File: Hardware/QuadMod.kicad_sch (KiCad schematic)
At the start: 30 parts, among them J6 SWD_Header, U1 STM32H563VIT, U2 AK4619VN, Y1 8MHz 20pF

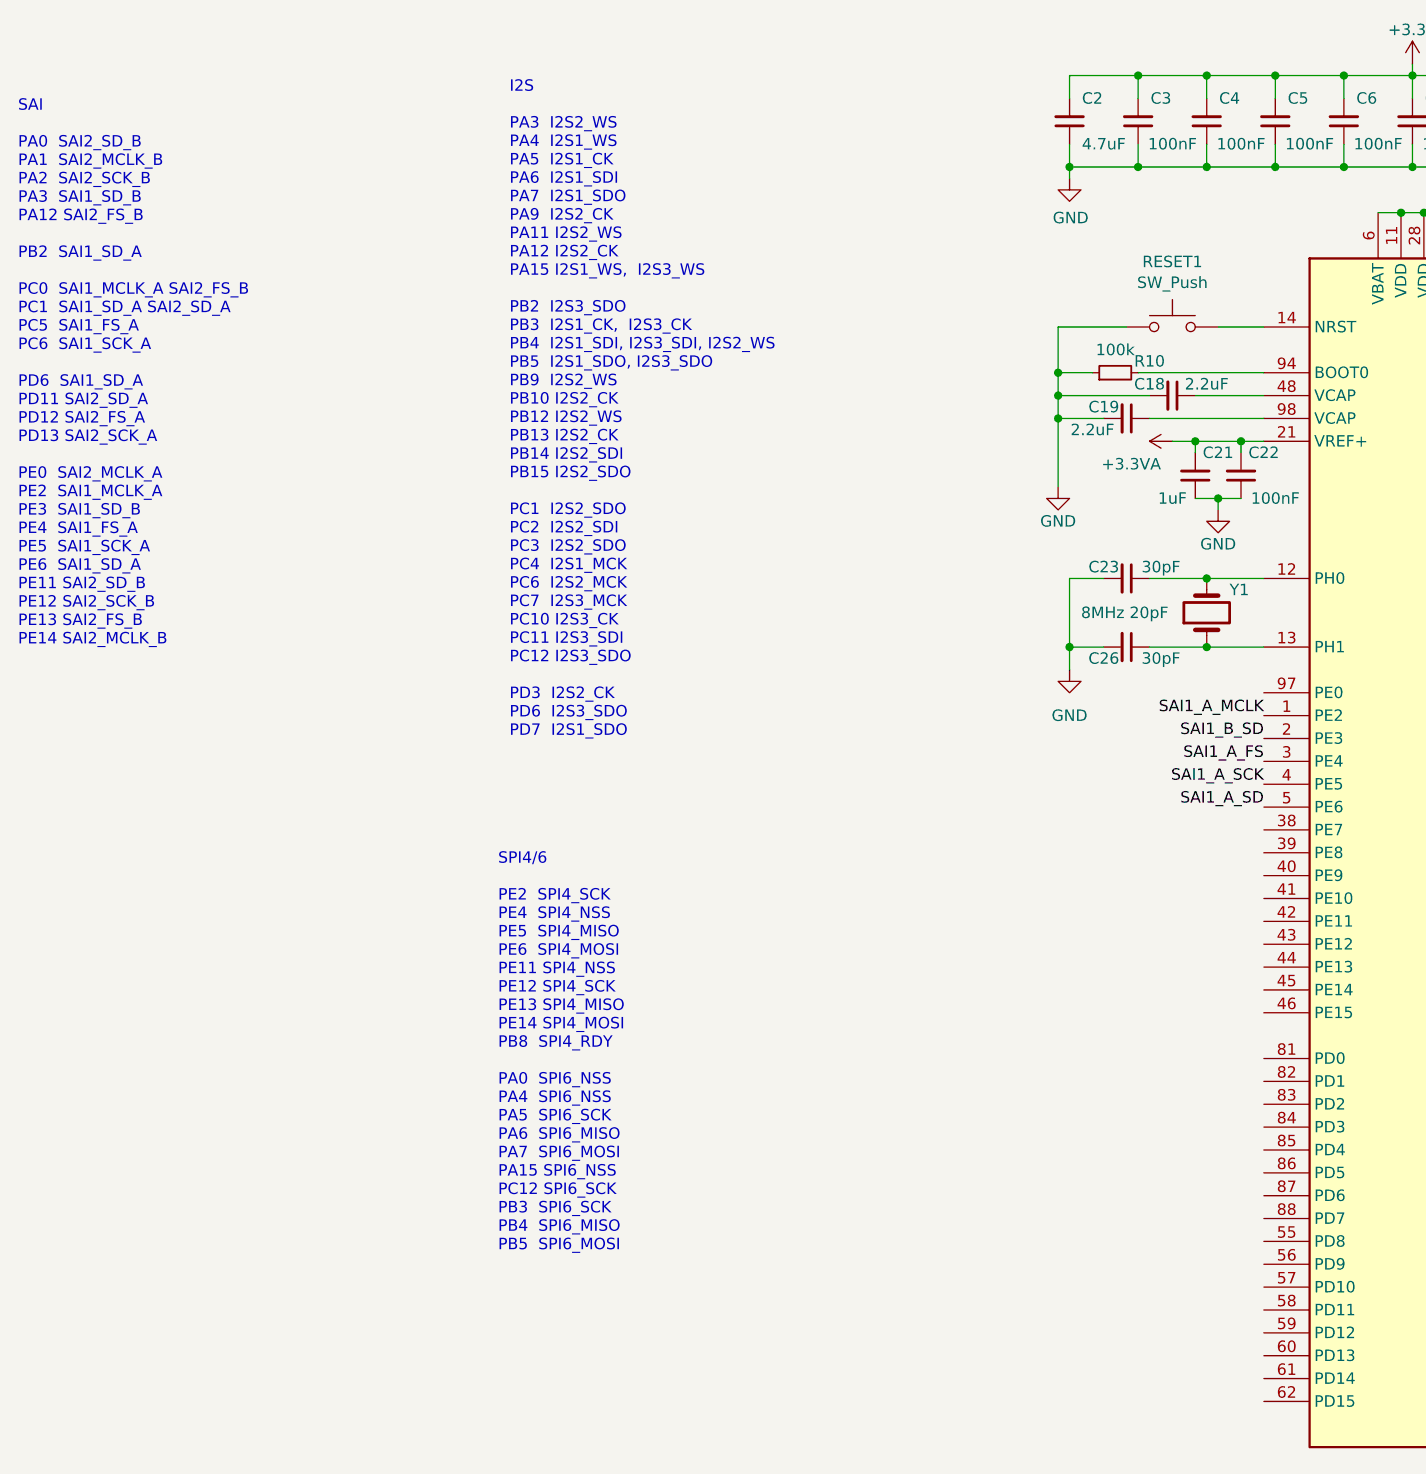
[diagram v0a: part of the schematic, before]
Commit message: Started configuring SAI2
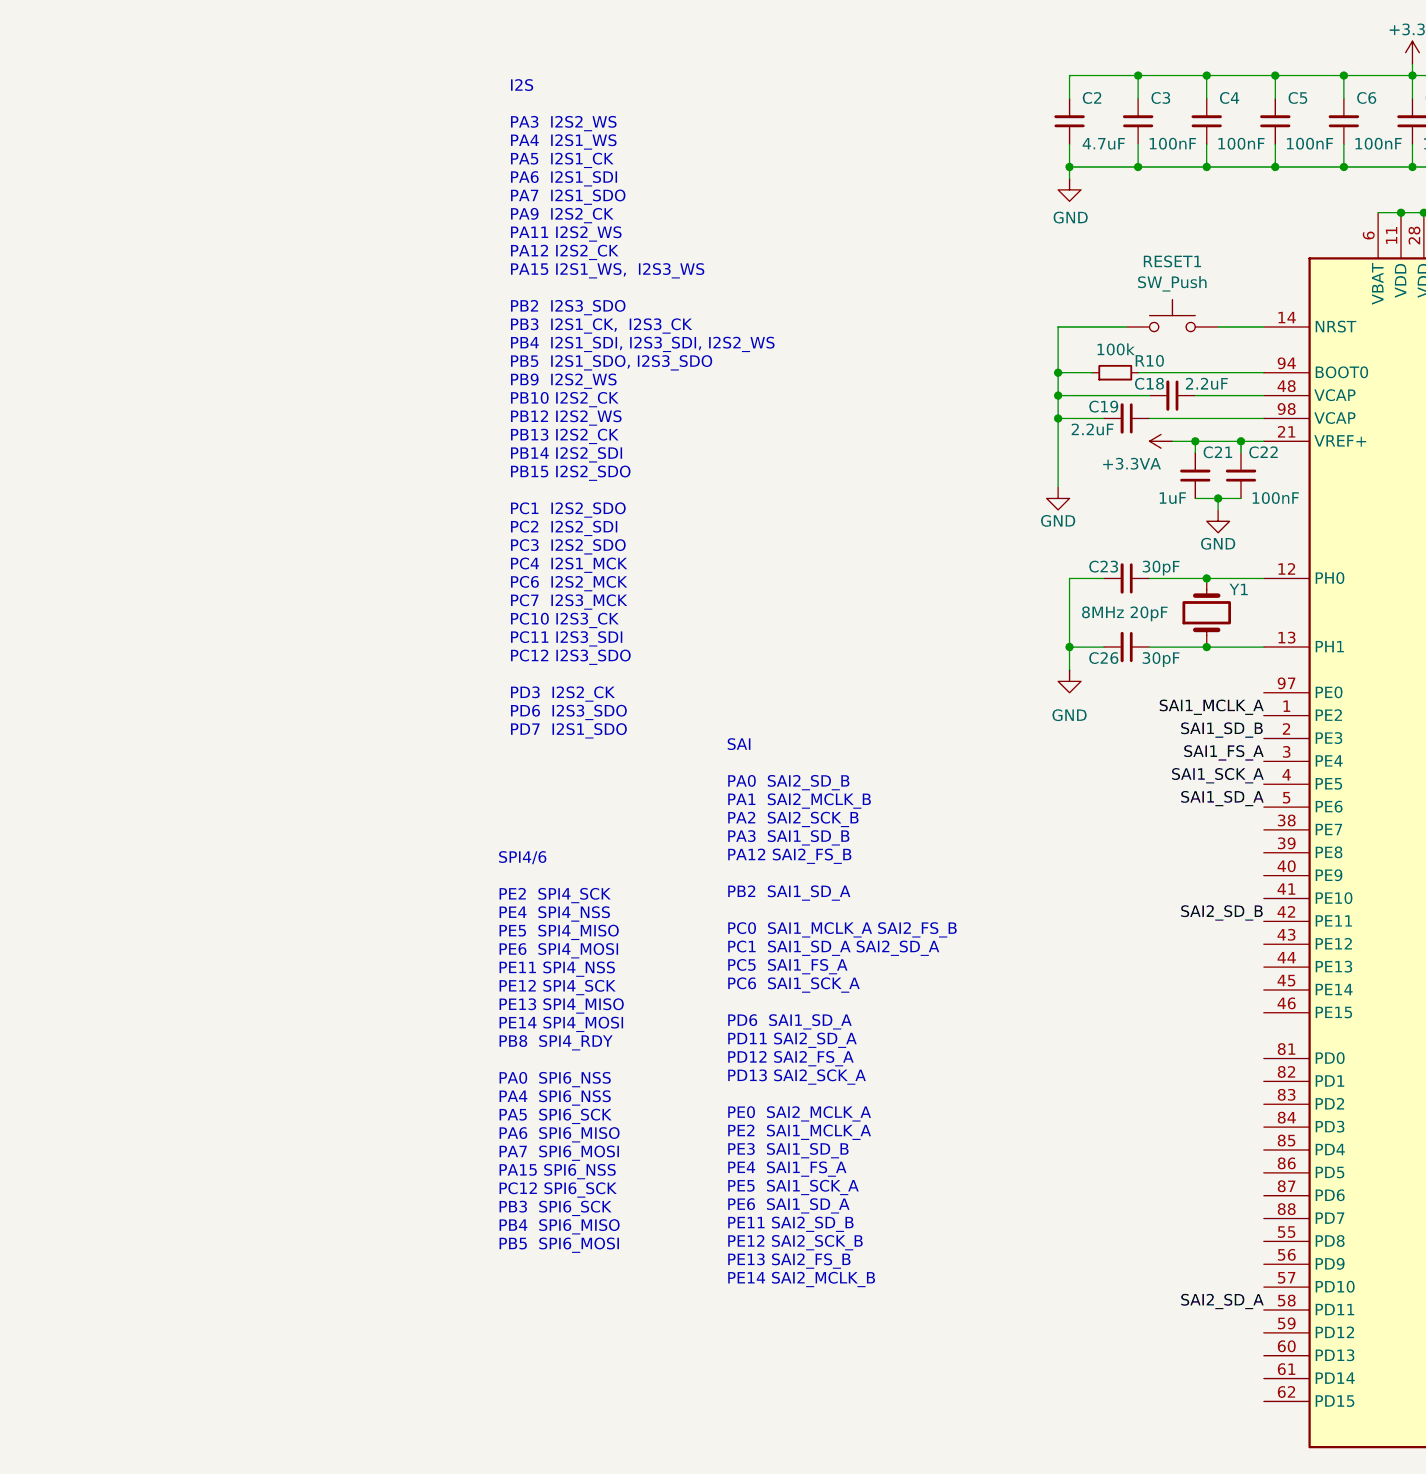
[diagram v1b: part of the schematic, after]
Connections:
- net SAI2_SD_B: now reaches U1.42 (PE11)
- net SAI2_SD_A: now reaches U1.58 (PD11)
- net SAI1_A_FS renamed SAI1_FS_A
- net SAI1_A_MCLK renamed SAI1_MCLK_A
- net SAI1_A_SCK renamed SAI1_SCK_A
- net SAI1_A_SD renamed SAI1_SD_A
- net SAI1_B_SD renamed SAI1_SD_B

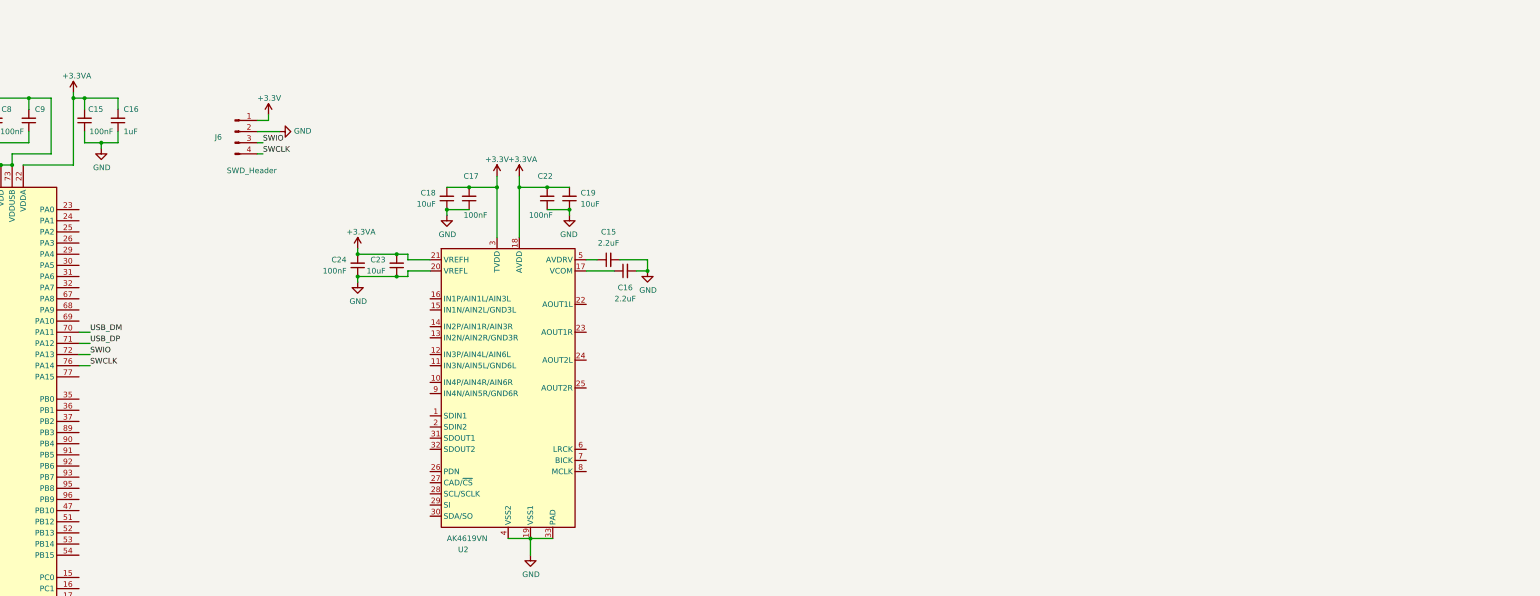
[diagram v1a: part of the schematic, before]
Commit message: Started laying out Audio Codec Test Board
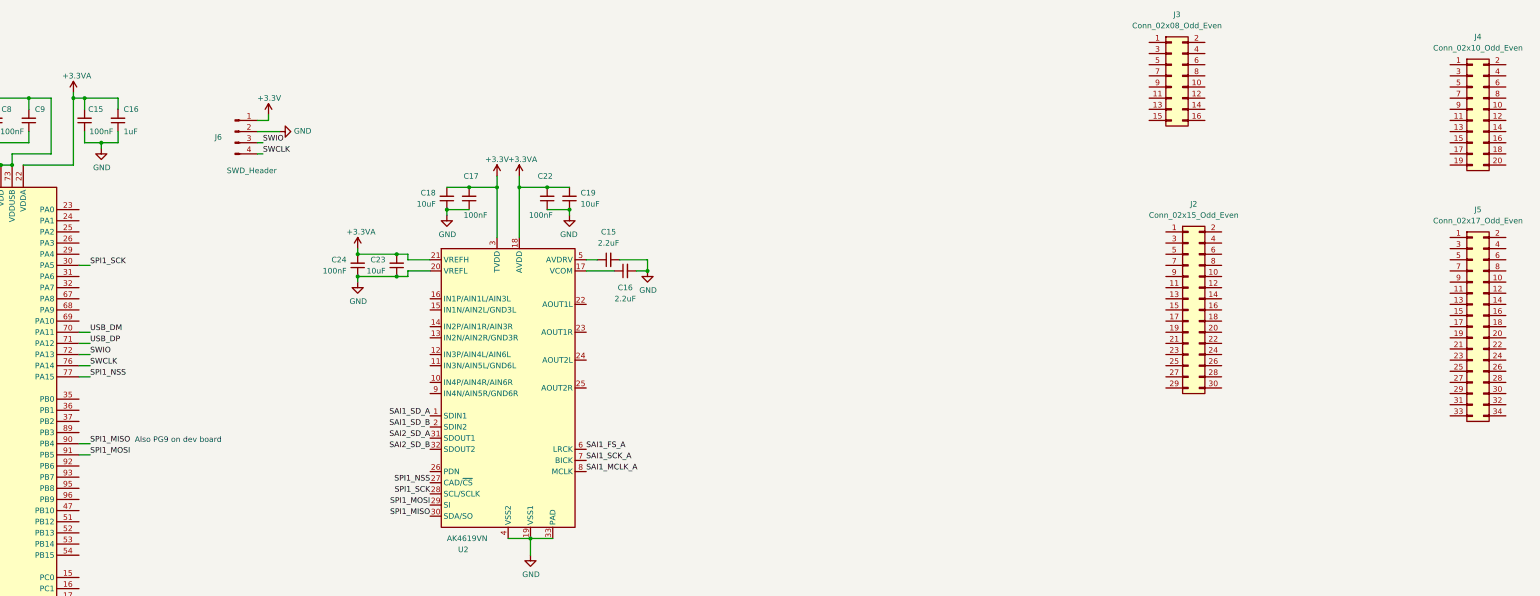
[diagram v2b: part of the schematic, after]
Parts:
- added J2: Conn_02x15_Odd_Even, symbol Connector_Generic:Conn_02x15_Odd_Even
- added J3: Conn_02x08_Odd_Even, symbol Connector_Generic:Conn_02x08_Odd_Even
- added J4: Conn_02x10_Odd_Even, symbol Connector_Generic:Conn_02x10_Odd_Even
- added J5: Conn_02x17_Odd_Even, symbol Connector_Generic:Conn_02x17_Odd_Even
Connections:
- net SAI1_FS_A: now also U2.6 (LRCK)
- net SAI1_MCLK_A: now also U2.8 (MCLK)
- net SAI1_SCK_A: now also U2.7 (BICK)
- net SAI1_SD_A: now also U2.1 (SDIN1)
- net SAI1_SD_B: now also U2.2 (SDIN2)
- net SAI2_SD_A: now also U2.31 (SDOUT1)
- net SAI2_SD_B: now also U2.32 (SDOUT2)
- net SPI1_NSS: now reaches U2.27 (CAD/~{CS})
- net SPI1_NSS: now also U1.77 (PA15)
- net SPI1_SCK: now reaches U2.28 (SCL/SCLK)
- net SPI1_SCK: now also U1.30 (PA5)
- net SPI1_MOSI: now reaches U2.29 (SI)
- net SPI1_MOSI: now also U1.91 (PB5)
- net SPI1_MISO: now reaches U2.30 (SDA/SO)
- net SPI1_MISO: now also U1.90 (PB4)
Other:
- note added: "Also PG9 on dev board"
